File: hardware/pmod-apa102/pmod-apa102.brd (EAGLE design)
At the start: 19.5 x 16 mm, 9 parts, among them J4 RA 6Pin SMD

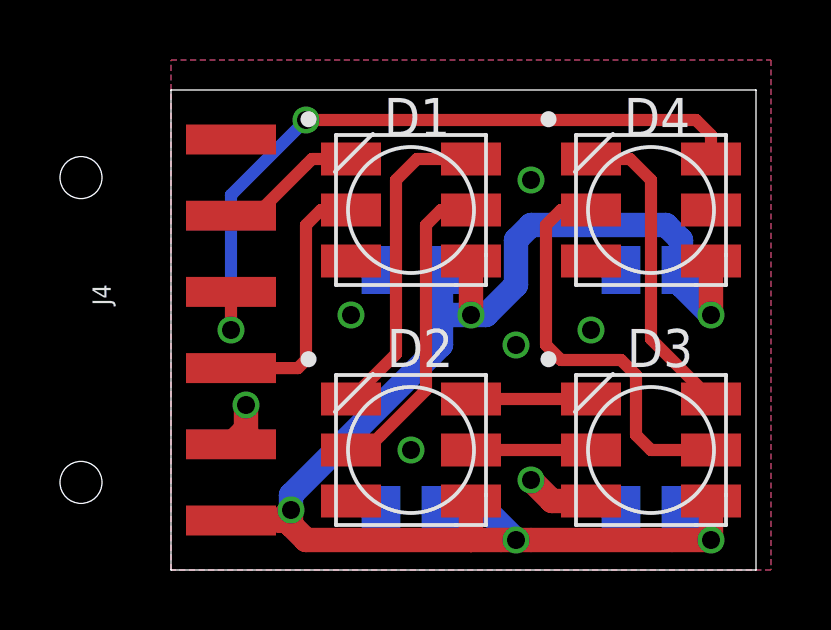
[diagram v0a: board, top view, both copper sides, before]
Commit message: APA102 PMD as submitted to Oshpark (minor silk fixups)
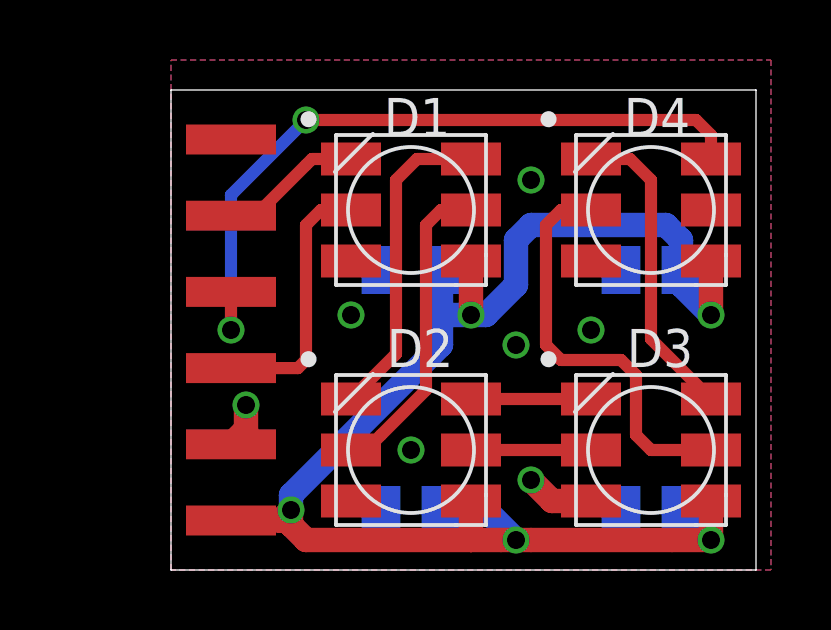
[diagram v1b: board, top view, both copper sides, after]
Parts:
- J4: device SparkFun-Connectors:1X06-SMD_RA_MALE -> mechanical:1X06-SMD_RA_MALE
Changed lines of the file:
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@@
 <attribute name="VALUE" x="6" y="7.9" size="1.27" layer="27" font="vector"/>
 </element>
-<element name="C1" library="rcl" package="C0805K" value="" x="8" y="10" rot="MR0"/>
-<element name="C2" library="rcl" package="C0805K" value="" x="8" y="2" rot="MR0"/>
-<element name="C3" library="rcl" package="C0805K" value="" x="16" y="2" rot="MR0"/>
+<element name="C1" library="rcl" package="C0805K" value="" x="8" y="10" smashed="yes" rot="MR0">
+<attribute name="NAME" x="5.625" y="10" size="1.27" layer="26" ratio="12" rot="MR270" align="center"/>
+<attribute name="VALUE" x="9" y="8.1" size="1.016" layer="28" rot="MR0"/>
+</element>
+<element name="C2" library="rcl" package="C0805K" value="" x="8" y="2" smashed="yes" rot="MR0">
+<attribute name="NAME" x="5.625" y="2.5" size="1.27" layer="26" ratio="12" rot="MR270" align="center"/>
+<attribute name="VALUE" x="9" y="0.1" size="1.016" layer="28" rot="MR0"/>
+</element>
+<element name="C3" library="rcl" package="C0805K" value="" x="16" y="2" smashed="yes" rot="MR0">
+<attribute name="NAME" x="13.625" y="2.5" size="1.27" layer="26" ratio="12" rot="MR270" align="center"/>
+<attribute name="VALUE" x="17" y="0.1" size="1.016" layer="28" rot="MR0"/>
+</element>
 <element name="C4" library="rcl" package="C0805K" value="" x="16" y="10" smashed="yes" rot="MR0">
-<attribute name="NAME" x="17" y="10.875" size="1.016" layer="26" rot="MR0"/>
+<attribute name="NAME" x="13.625" y="10" size="1.27" layer="26" ratio="12" rot="MR270" align="center"/>
 <attribute name="VALUE" x="17" y="8.1" size="1.016" layer="28" rot="MR0"/>
 </element>
-<element name="J4" library="SparkFun-Connectors" package="1X06-SMD_RA_MALE" value="RA 6Pin SMD" x="-3" y="8" rot="R270">
+<element name="J4" library="mechanical" package="1X06-SMD_RA_MALE" value="RA 6Pin SMD" x="-3" y="8" smashed="yes" rot="R270">
 <attribute name="PROD_ID" value="CONN-08971" x="15" y="24" size="1.778" layer="27" rot="R270" display="off"/>
+<attribute name="VALUE" x="-4.016" y="9.651" size="0.6096" layer="27" font="vector" ratio="20" rot="R270"/>
 </element>
 </elements>
